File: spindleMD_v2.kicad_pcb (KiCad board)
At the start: 2 copper layers, 72 x 95 mm, 100 parts, among them J1 Conn_LogicPower, J2 Conn_SWD, J3 Conn_UART, J4 Conn_I2C, J5 Conn_Encoder, J6 Conn_GPIO, J7 Conn_MotorPower, J8 Conn_drivePower, J9 Conn_Motor, Q1 Q_NMOS_GDS, Q2 Q_NMOS_GDS, Q3 Q_NMOS_GDS, Q4 Q_NMOS_GDS, SW1 USER_BUTTON, SW2 RESET_BUTTON, U1 L7805, U10 ADuM3190, U2 L78L33_SOT89, U3 IK0505SA, U4 STM32F303K8Tx, U5 TLP152, U6 TLP152, U7 TLP152, U8 TLP152, U9 ACS712xLCTR-30A

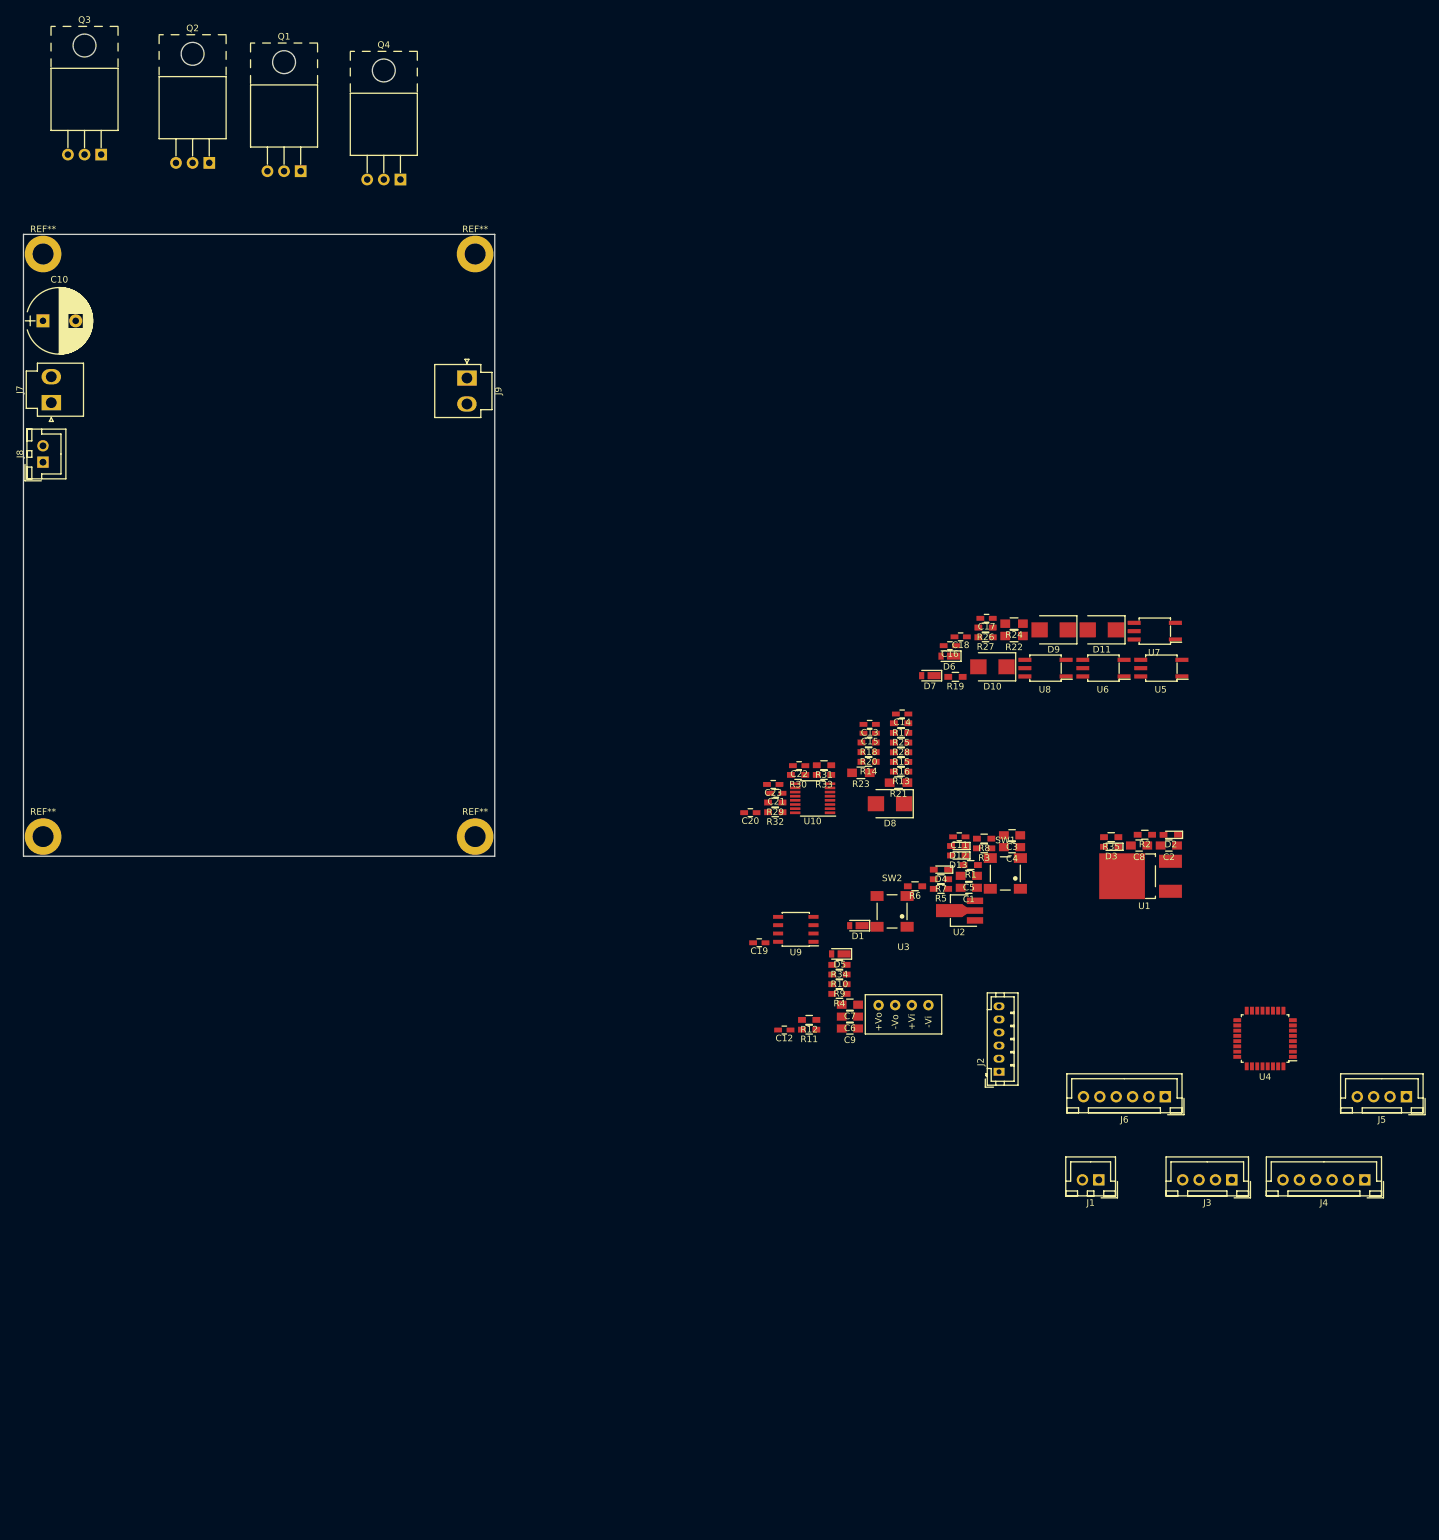
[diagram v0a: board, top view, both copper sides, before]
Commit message: 電流センサ電源パスコン追加
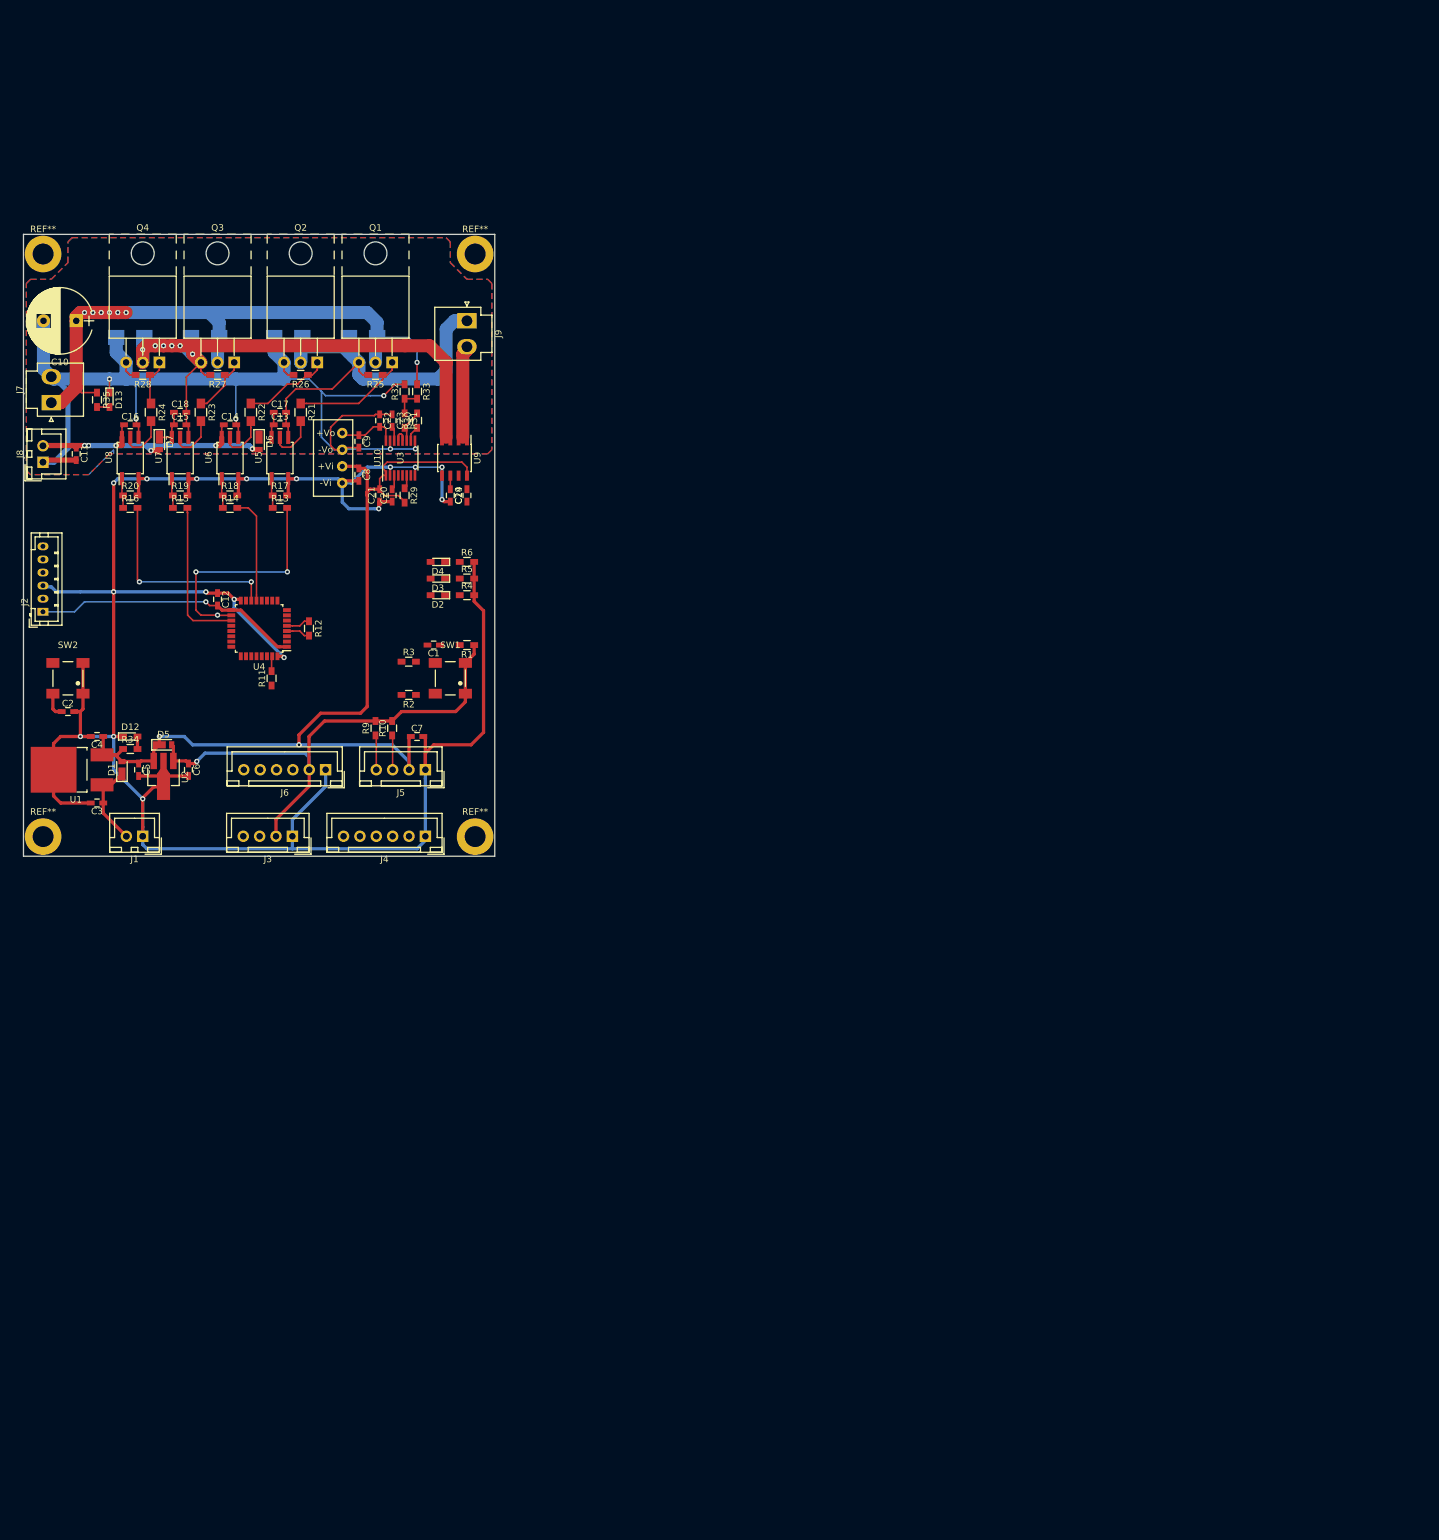
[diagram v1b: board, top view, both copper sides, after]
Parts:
- removed R7, R8: 2k, Resistors_SMD:R_0603_HandSoldering
- added C24: 0.1u, Capacitors_SMD:C_0603_HandSoldering, F.Cu at (31.8, -7.62)
- C1, C2, C3, C4, C5, C6, C7, C8, C9: footprint Capacitors_SMD:C_0805_HandSoldering -> Capacitors_SMD:C_0603_HandSoldering
- D10, D11, D8, D9: moved to B.Cu
- moved C2 169.4 mm to (-29.2, 25.4), turned to 0 degrees
- moved R35 168.7 mm to (-24.8, -22.2), turned to 270 degrees
- moved U4 166.0 mm to (0.00, 12.7)
- moved U1 164.0 mm to (-28.6, 34.3)
- moved J2 162.1 mm to (-33.0, 10.2)
- moved J5 158.0 mm to (25.4, 34.3)
- moved J1 155.2 mm to (-17.8, 44.5)
- moved D11 155.0 mm to (-19.7, -31.8)
- moved J3 152.8 mm to (5.08, 44.5)
- moved J4 152.8 mm to (25.4, 44.5)
- moved U7 151.2 mm to (-12.1, -13.3), turned to 90 degrees
- moved D13 147.2 mm to (-22.9, -22.2), turned to 270 degrees
- moved C11 147.0 mm to (-27.9, -14.0), turned to 270 degrees
- moved U8 143.5 mm to (-19.7, -13.3), turned to 90 degrees
- moved C4 140.8 mm to (-24.8, 29.2)
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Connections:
- J7 pad 1: GNDPWR -> VDD
- J7 pad 2: VDD -> GNDPWR
- J9 pad 1: /CurrentSensing/IP+ -> /H-Bridge/AOUT
- J9 pad 2: /H-Bridge/AOUT -> /CurrentSensing/IP+
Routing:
- net GND: track 0.00 -> 365.8 mm, vias 0 -> 17
- net GNDPWR: track 0.00 -> 169.6 mm, vias 0 -> 6
- net +5V: track 0.00 -> 145.7 mm, vias 0 -> 2
- net +3V3: track 0.00 -> 123.4 mm, vias 0 -> 2
- net VDD: track 0.00 -> 101.5 mm, vias 0 -> 7
- net /H-Bridge/BOUT: track 0.00 -> 89.1 mm, vias 0 -> 6
- net /H-Bridge/AOUT: track 0.00 -> 66.8 mm
- net +12V: track 0.00 -> 44.7 mm, vias 0 -> 6
- net /H-Bridge/GATE_AP: track 0.00 -> 35.3 mm, vias 0 -> 3
- net /H-Bridge/GATE_BN: track 0.00 -> 31.4 mm, vias 0 -> 2
- net /H-Bridge/GATE_BP: track 0.00 -> 23.4 mm
- net Net-(Q1-Pad1): track 0.00 -> 17.7 mm
- net /H-Bridge/GATE_AN: track 0.00 -> 16.4 mm
- net /CurrentSensing/IP+: track 0.00 -> 14.1 mm
- net Net-(Q2-Pad1): track 0.00 -> 13.4 mm
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- added copper zone on B.Cu, net GNDPWR
- added copper zone on F.Cu, net GNDPWR
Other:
- net class HighCurrent added: clearance 0.5, trace_width 2, via_dia 0.8, via_drill 0.4
- net class LowCurrent added: clearance 0.2, trace_width 0.5, via_dia 0.8, via_drill 0.4

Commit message: アートワーク完成
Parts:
- moved J9 147.4 mm to (131.8, 74.0)
- moved C1 141.4 mm to (126.7, 115.2)
- moved C10 141.4 mm to (72.1, 65.7)
- moved C11 141.4 mm to (72.1, 86.0)
- moved C12 141.4 mm to (93.7, 108.3)
- moved C13 141.4 mm to (103.2, 81.6)
- moved C14 141.4 mm to (95.6, 81.6)
- moved C15 141.4 mm to (87.9, 81.6)
- moved C16 141.4 mm to (80.3, 81.6)
- moved C17 141.4 mm to (103.2, 79.7)
- moved C18 141.4 mm to (87.9, 79.7)
- moved C19 141.4 mm to (129.2, 92.4)
- moved C2 141.4 mm to (70.8, 125.4)
- moved C20 141.4 mm to (120.3, 92.4)
- moved C21 141.4 mm to (118.4, 92.4)
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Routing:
- net GND: track 365.8 -> 1062.1 mm, vias 17 -> 164
- net GNDPWR: track 169.6 -> 500.7 mm, vias 6 -> 76
- net /MCU/NRST: track 7.51 -> 82.5 mm, vias 0 -> 2
- net /MCU/SD_Monitor: track 0.00 -> 52.1 mm, vias 0 -> 2
- net /MCU/SHUTDOWN: track 0.00 -> 51.7 mm, vias 0 -> 2
- net /MCU/SWO: track 0.00 -> 50.7 mm, vias 0 -> 3
- net /MCU/RE_B: track 5.30 -> 52.2 mm
- net /MCU/RE_A: track 5.28 -> 52.0 mm
- net /MCU/LED2: track 0.00 -> 45.9 mm, vias 0 -> 4
- net /MCU/I2C_SCL: track 0.00 -> 44.7 mm, vias 0 -> 2
- net /MCU/LED3: track 0.00 -> 42.5 mm, vias 0 -> 4
- net /MCU/I2C_SDA: track 0.00 -> 41.7 mm, vias 0 -> 2
- net /MCU/I_SENSE: track 0.00 -> 41.3 mm, vias 0 -> 2
- net /MCU/USER_BUTTON: track 0.00 -> 39.4 mm, vias 0 -> 2
- net /MCU/LED1: track 0.00 -> 39.2 mm, vias 0 -> 4
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- added copper zone on B.Cu, net GND
- added copper zone on F.Cu, net GND
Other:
- outline, holes or cut-outs redrawn
